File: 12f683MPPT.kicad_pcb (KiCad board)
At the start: 2 copper layers, 98.3 x 72.6 mm, 54 parts, among them J1 Conn_01x01_Male, J2 Conn_01x01_Male, J3 Conn_01x01_Male, J4 Conn_01x01_Male, Q1 BUK9511-55A127, Q2 BUK9511-55A127, Q3 2N2222A, Q4 2N2222A, Q5 2N2907A, SW1 SW_Push, U1 LM7805_TO220, U2 PIC12F683-IP, U3 LM358

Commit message: Update circuit.
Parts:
- added J5: Vin, Connector_Pin:Pin_D1.0mm_L10.0mm, F.Cu at (55.4, 44.3)
- added J6: GND, Connector_Pin:Pin_D1.0mm_L10.0mm, F.Cu at (55.4, 48.5)
- added J7: 12V, Connector_Pin:Pin_D1.0mm_L10.0mm, F.Cu at (55.2, 56.4)
- C1, C7: footprint Capacitors_THT:CP_Radial_D12.5mm_P5.00mm -> Capacitor_THT:CP_Radial_D12.5mm_P5.00mm
- C2, C3, C5: footprint Capacitors_THT:CP_Radial_D12.5mm_P5.00mm -> Capacitor_THT:CP_Radial_D8.0mm_P2.50mm
- C4: footprint Capacitors_THT:C_Disc_D7.5mm_W4.4mm_P5.00mm -> Capacitor_THT:C_Disc_D7.5mm_W4.4mm_P5.00mm
- D1 (x2), D2 (x2), D6 (x2): footprint Diodes_THT:D_DO-201AD_P15.24mm_Horizontal -> Diode_THT:D_DO-201AD_P15.24mm_Horizontal
- D4, D7, D8: footprint LEDs:LED_D3.0mm -> LED_THT:LED_D3.0mm
- D5: footprint Diodes_THT:D_DO-41_SOD81_P10.16mm_Horizontal -> Diode_THT:D_DO-41_SOD81_P10.16mm_Horizontal
- D9: footprint Diode_THT:D_DO-41_SOD81_P10.16mm_Horizontal -> Diode_THT:D_DO-41_SOD81_P5.08mm_Vertical_AnodeUp
- L1: footprint Inductors_THT:L_Toroid_Vertical_L16.0mm_W8.0mm_P7.62mm -> Inductor_THT:L_Toroid_Vertical_L16.0mm_W8.0mm_P7.62mm
- Q3, Q4, Q5: footprint TO_SOT_Packages_THT:TO-92_Inline_Wide -> Package_TO_SOT_THT:TO-92_Inline_Wide
- R1, R10, R11, R12, R13, R14, R15, R16, R2, R3, R4, R5, R6, R7, R8, R9: footprint Resistors_THT:R_Axial_DIN0309_L9.0mm_D3.2mm_P12.70mm_Horizontal -> Resistor_THT:R_Axial_DIN0309_L9.0mm_D3.2mm_P12.70mm_Horizontal
- U1: footprint TO_SOT_Packages_THT:TO-220-3_Vertical -> Package_TO_SOT_THT:TO-220-3_Vertical
- U2, U3: footprint Housings_DIP:DIP-8_W7.62mm_LongPads -> Package_DIP:DIP-8_W7.62mm_LongPads
- moved D9 18.7 mm to (119.2, 32.5), turned to 0 degrees
- moved C5 9.93 mm to (104.4, 59.6)
- moved D2 8.15 mm to (104.5, 70.9)
- moved D2 8.07 mm to (110.5, 70.9)
- moved R8 7.52 mm to (55.6, 60.8)
- moved R16 7.35 mm to (68.3, 64.7)
- moved U1 5.09 mm to (59.4, 56.4)
- moved C2 3.74 mm to (106.8, 49.4)
- moved R12 3.71 mm to (47.0, 61.5)
- moved C3 2.58 mm to (72.4, 51.7)
- moved J4 2.58 mm to (120.2, 78.0)
- moved J2 2.53 mm to (42.0, 67.5)
- moved D4 2.17 mm to (57.2, 89.3)
- moved R6 2.09 mm to (57.2, 81.0)
- moved D6 1.75 mm to (60.6, 39.3)
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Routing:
- net PRI_LO: track 98.8 -> 130.9 mm
- net Net-(D1-K): track 44.6 -> 65.2 mm
- net Net-(D6-K): track 62.4 -> 75.8 mm
- net +24V: track 35.9 -> 48.5 mm
- net Net-(D9-K): track 31.8 -> 20.1 mm
- net GNDPWR: track 319.0 -> 310.1 mm
- net /PV-Voltage: track 3.11 -> 11.2 mm
- net Net-(R12-Pad1): track 19.7 -> 12.5 mm
- net Net-(D1-A): track 45.4 -> 38.5 mm
- net Net-(U3B--): track 18.0 -> 11.9 mm
- net PRI_HI: track 49.6 -> 44.7 mm
- net Net-(D3-A): track 97.2 -> 92.4 mm
- net /BootStrap: track 33.6 -> 30.2 mm
- net Net-(D5-K): track 5.54 -> 8.13 mm
- net Net-(U2-GP5): track 28.6 -> 27.2 mm
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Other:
- board text added: "MPPT"

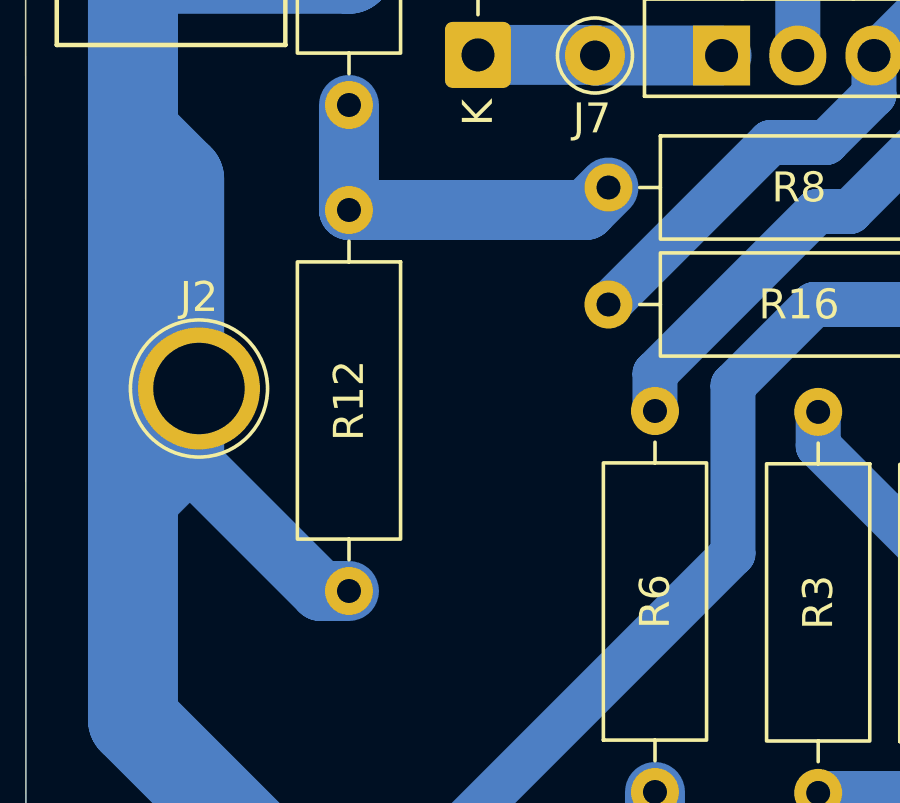
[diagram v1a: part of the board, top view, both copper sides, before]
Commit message: Add zener for input voltage limiting.
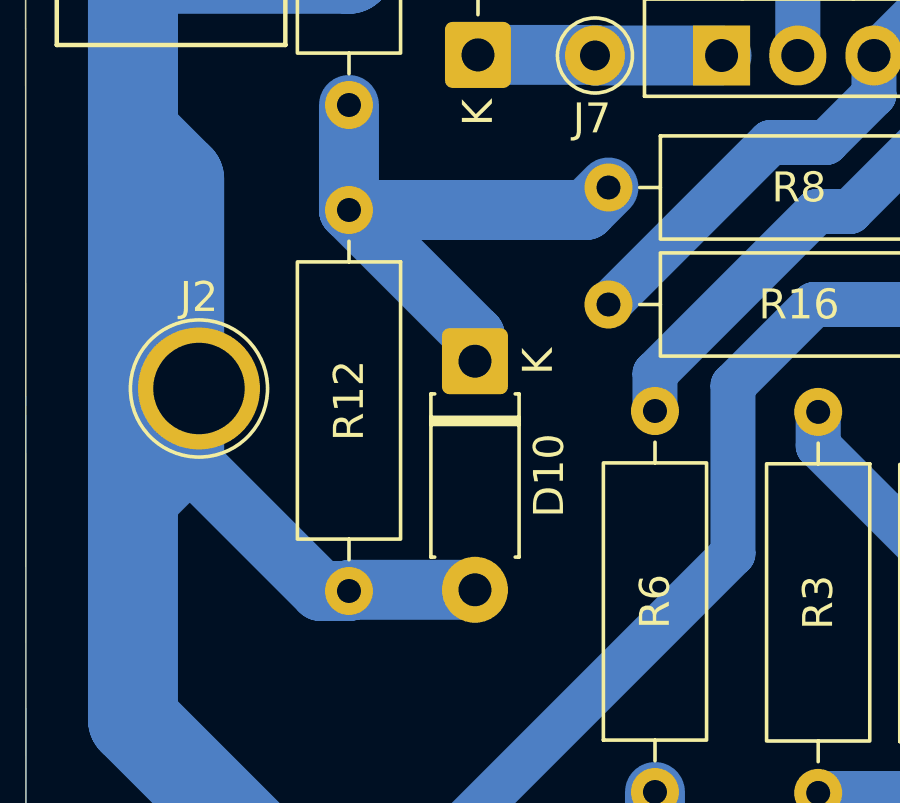
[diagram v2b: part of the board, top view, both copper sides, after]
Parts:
- added D10: 1N5227B, Diode_THT:D_DO-41_SOD81_P7.62mm_Horizontal, F.Cu at (51.2, 66.6)
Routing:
- net Net-(D10-K): track 12.5 -> 19.2 mm
- net GNDPWR: track 310.1 -> 314.3 mm

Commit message: Update PCB files.
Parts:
- D10: footprint Diode_THT:D_DO-41_SOD81_P7.62mm_Horizontal -> Diode_THT:D_DO-41_SOD81_P12.70mm_Horizontal
- REF** (x4): value MountingHole_3.2mm_M3_Pad -> MountingHole_4.3mm_M4_DIN965_Pad; footprint MountingHole:MountingHole_3.2mm_M3_Pad -> MountingHole:MountingHole_4.3mm_M4_DIN965_Pad
- moved R11 18.8 mm to (83.0, 64.5), turned to 0 degrees
- moved R9 13.5 mm to (78.5, 37.6)
- moved Q3 10.3 mm to (91.2, 50.5)
- moved C2 5.93 mm to (101.0, 48.1)
- moved D10 5.74 mm to (51.3, 60.9)
- moved D8 5.24 mm to (92.0, 89.3), turned to 0 degrees
- moved SW1 4.40 mm to (47.0, 85.3)
- moved R13 4.26 mm to (87.3, 86.7)
- moved R14 4.02 mm to (94.6, 68.2)
- moved R1 3.85 mm to (74.7, 81.0)
- moved R15 3.80 mm to (90.7, 81.0)
- moved J2 3.47 mm to (39.7, 64.9)
- moved D3 3.46 mm to (88.7, 42.5)
- moved C5 3.43 mm to (101.1, 58.5), turned to 0 degrees
- moved OUT1 3.33 mm to (128.2, 79.1)
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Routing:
- net GNDPWR: track 314.3 -> 406.2 mm
- net Net-(D3-A): track 92.4 -> 59.3 mm
- net /BootStrap: track 30.2 -> 51.1 mm
- net Net-(D1-A): track 38.5 -> 55.5 mm
- net Net-(Q3-C): track 19.6 -> 7.82 mm
- net /PV-Current: track 48.8 -> 38.1 mm
- net +24V: track 48.5 -> 58.5 mm
- net PRI_LO: track 130.9 -> 139.0 mm
- net Net-(D10-K): track 19.2 -> 11.4 mm
- net Net-(U2-GP3): track 47.6 -> 42.9 mm
- net PRI_HI: track 44.7 -> 40.1 mm
- net /3.6v: track 61.0 -> 57.6 mm
- net Net-(U2-GP2): track 10.3 -> 13.6 mm
- net Net-(D6-K): track 75.8 -> 73.2 mm
- net Net-(U3B--): track 11.9 -> 14.1 mm
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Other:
- board size 98.3 x 72.6 mm -> 97.8 x 72.6 mm
- board text added: "K"

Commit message: More PCB files changes.
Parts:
- moved R9(2.2k) 6.15 mm to (84.7, 37.5)
- renumbered C1 to C1(100u), C2 to C2(4.7u), C3 to C3(100u), C4 to C4(0.1u), C5 to C5(10u), C7 to C7(47u), D10 to D10(1N5227B), D3 to D3(1N5819), D9 to D9(1N5733A), J1 to J1(+), J2 to J2(-), J3 to J3(-), J4 to J4(+), J5 to J5(Vin), J6 to J6(GND), J7 to J7(12V), U3 to LM358, U1 to LM7805, U2 to PIC12F683, Q1 to Q1(BUK9511-55A), Q2 to Q2(BUK9511-55A), Q3 to Q3(2N2222A), Q4 to Q4(2N2222A), Q5 to Q5(2N2907A), R1 to R1(1k), R10 to R10(1k), R11 to R11(10k), R12 to R12(47k), R13 to R13(10k), R14 to R14(4.7k), R15 to R15(3.3k), R16 to R16(10k), R2 to R2(100k), R3 to R3(10k), R4 to R4(100k), R5 to R5(300k), R6 to R6(1k), R7 to R7(1k), R8 to R8(100k), R9 to R9(2.2k)
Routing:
- net /BootStrap: track 51.1 -> 44.1 mm
- net Net-(Q3-C): track 7.82 -> 11.6 mm

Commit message: Update PCB files.
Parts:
- R10(1k), R9(2.2k): footprint Resistor_THT:R_Axial_DIN0309_L9.0mm_D3.2mm_P12.70mm_Horizontal -> Resistor_THT:R_Axial_DIN0309_L9.0mm_D3.2mm_P5.08mm_Vertical
- moved R9(2.2k) 11.4 mm to (95.7, 40.3), turned to -90 degrees
- moved R10(1k) 9.49 mm to (95.7, 36.6)
- moved C4(0.1u) 1.41 mm to (78.5, 47.8)
- moved D3(1N5819) 1.20 mm to (88.7, 41.3)
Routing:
- net /BootStrap: track 44.1 -> 26.7 mm
- net Net-(Q4-B): track 8.15 -> 18.3 mm
- net Net-(Q3-C): track 11.6 -> 19.9 mm
- net Net-(D6-K): track 73.2 -> 77.6 mm
- net Net-(D3-A): track 59.3 -> 60.2 mm
- net GNDPWR: track 406.2 -> 407.0 mm
